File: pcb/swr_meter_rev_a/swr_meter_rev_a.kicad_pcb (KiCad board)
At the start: 2 copper layers, 51.5 x 77 mm, 26 parts, among them P1 BNC, P2 BNC, SW1 Double switch, SW2 2 pos. switch

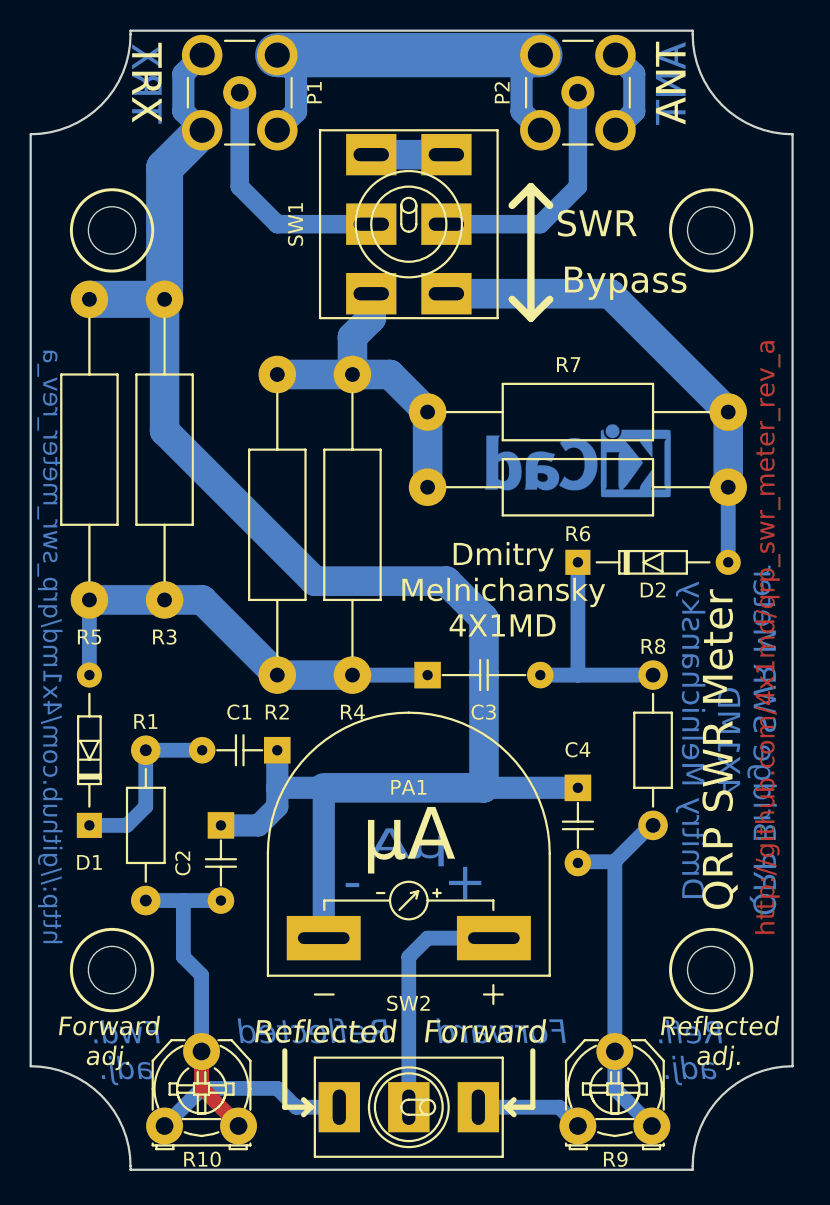
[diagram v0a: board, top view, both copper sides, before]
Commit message: Corrected URLs on the PCB.
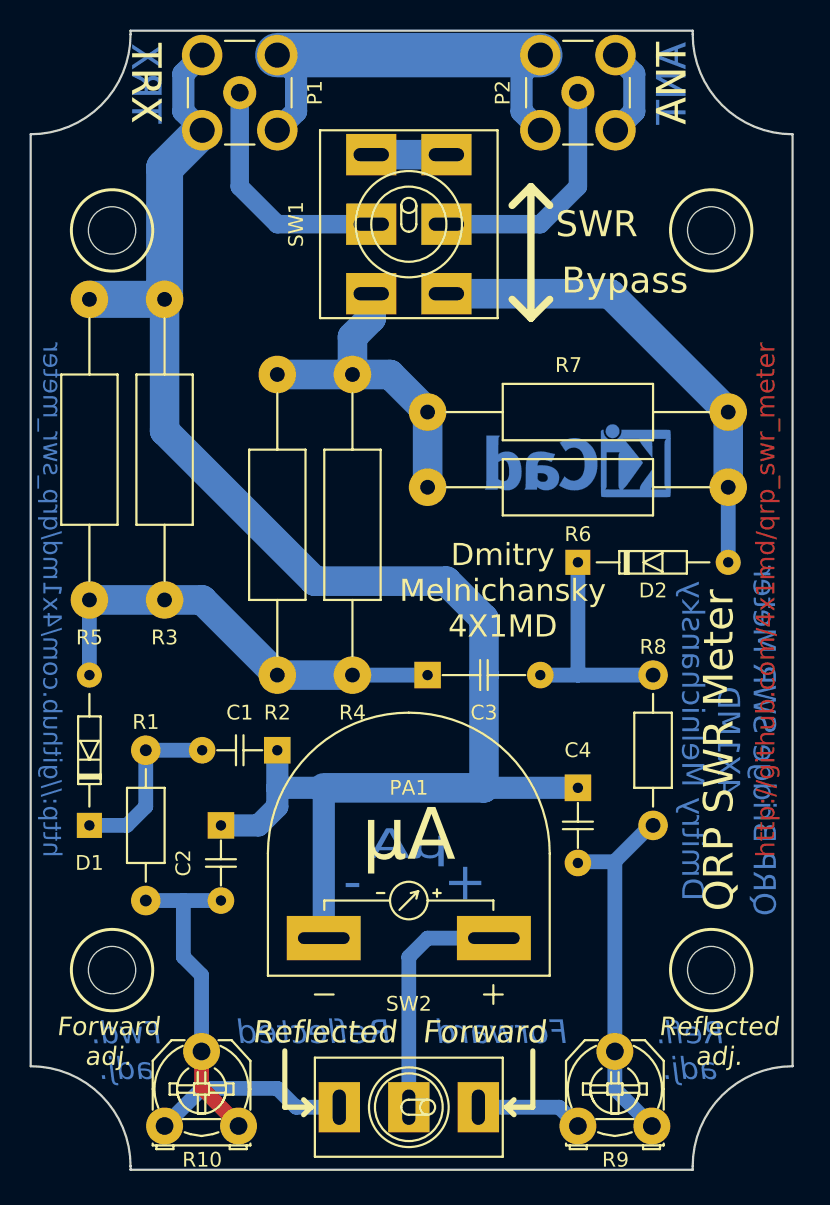
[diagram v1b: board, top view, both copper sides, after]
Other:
- board text added: "http://github.com/4x1md/qrp_swr_meter"
- board text removed: "http://github.com/4x1md/qrp_swr_meter_rev_a"
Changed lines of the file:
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@@
     (links 41)
     (no_connects 2)
-    (area 117.821429 65.374999 169.578571 143.061)
+    (area 117.874999 65.584999 169.525001 142.735001)
     (thickness 1.6)
     (drawings 88)
@@
     (effects (font (size 2 2) (thickness 0.3)))
   )
-  (gr_text http://github.com/4x1md/qrp_swr_meter_rev_a (at 167.64 106.68 90) (layer F.Cu)
+  (gr_text http://github.com/4x1md/qrp_swr_meter (at 167.64 104.14 90) (layer F.Cu)
     (effects (font (size 1.25 1.25) (thickness 0.25)))
   )
@@
     (effects (font (size 2 2) (thickness 0.4)) (justify mirror))
   )
-  (gr_text http://github.com/4x1md/qrp_swr_meter_rev_a (at 119.38 107.315 270) (layer B.Cu)
+  (gr_text http://github.com/4x1md/qrp_swr_meter (at 119.38 104.14 270) (layer B.Cu)
     (effects (font (size 1.25 1.25) (thickness 0.25)) (justify mirror))
   )

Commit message: Silkprint corrections and new gerbers.
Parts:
- moved R8 2.54 mm to (160.0, 111.8)
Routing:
- net Net-(C4-Pad2): track 25.1 -> 24.0 mm
- net Net-(C3-Pad2): track 15.1 -> 16.2 mm
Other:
- board text added: "QRP SWR Meter Rev. A"
- board text removed: "Dmitry Melnichansky 4X1MD"
- board text removed: "QRP SWR Meter"
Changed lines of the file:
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@@
     (area 117.874999 65.584999 169.525001 142.735001)
     (thickness 1.6)
-    (drawings 88)
-    (tracks 89)
+    (drawings 87)
+    (tracks 90)
     (zones 0)
     (modules 26)
@@
   )
   (setup
-    (last_trace_width 0.25)
+    (last_trace_width 1)
     (user_trace_width 0.5)
     (user_trace_width 0.75)
@@
   (module custom_kicad_footprints:Microampermeter (layer F.Cu)
     (at 143.51 127)
-    (fp_text reference PA1 (at 0 -10.16) (layer F.SilkS)
+    (fp_text reference PA1 (at 0 3.81) (layer F.SilkS)
       (effects (font (size 1 1) (thickness 0.15)))
     )
@@
   )
   (module Resistors_ThroughHole:Resistor_Horizontal_RM10mm (layer F.Cu)
-    (at 160.02 109.22 270)
+    (at 160.02 111.76 270)
     (descr "Resistor, Axial,  RM 10mm, 1/3W")
     (tags "Resistor Axial RM 10mm 1/3W")
@@
     (descr "Tumbler Switch x2")
     (tags "SWITCH DEV TOGGLE ILLUM SPDT")
-    (fp_text reference SW2 (at 0 6.985 360) (layer F.SilkS)
+    (fp_text reference SW2 (at 6.985 2 270) (layer F.SilkS)
       (effects (font (size 1 1) (thickness 0.15)))
     )
@@
     (descr "Tumbler Switch x2")
     (tags "SWITCH DEV TOGGLE ILLUM SPDT")
-    (fp_text reference SW1 (at 0 7.62 270) (layer F.SilkS)
+    (fp_text reference SW1 (at -7.62 0 360) (layer F.SilkS)
       (effects (font (size 1 1) (thickness 0.15)))
     )
@@
     (descr "Diode, DO-35,  SOD27, Horizontal, RM 10mm")
     (tags "Diode, DO-35, SOD27, Horizontal, RM 10mm, 1N4148,")
-    (fp_text reference D2 (at 5.08 1.905) (layer F.SilkS)
+    (fp_text reference D2 (at 5.08 -1.905) (layer F.SilkS)
       (effects (font (size 1 1) (thickness 0.15)))
     )
@@
     (descr "Resistor, Axial, RM 20mm,")
     (tags "Resistor Axial RM 20mm")
-    (fp_text reference R2 (at 22.86 0 360) (layer F.SilkS)
+    (fp_text reference R2 (at -2.54 0 360) (layer F.SilkS)
       (effects (font (size 1 1) (thickness 0.15)))
     )
@@
     (descr "Resistor, Axial, RM 20mm,")
     (tags "Resistor Axial RM 20mm")
-    (fp_text reference R4 (at 22.86 0 360) (layer F.SilkS)
+    (fp_text reference R4 (at -2.54 0 360) (layer F.SilkS)
       (effects (font (size 1 1) (thickness 0.15)))
     )
@@
     (descr "Resistor, Axial, RM 20mm,")
     (tags "Resistor Axial RM 20mm")
-    (fp_text reference R7 (at 10.795 3.175 180) (layer F.SilkS)
+    (fp_text reference R7 (at 10.16 3.175 180) (layer F.SilkS)
       (effects (font (size 1 1) (thickness 0.15)))
     )
@@
       (xy -2.537313 2.939947) (xy -2.454562 2.96715) (xy -2.376928 2.977424) (xy -2.273043 2.973429)) (layer B.Cu) (width 0.01))
   )
+  (gr_line (start 152.4 83.185) (end 151.765 85.09) (angle 90) (layer F.SilkS) (width 0.5))
+  (gr_line (start 151.13 83.185) (end 151.765 85.09) (angle 90) (layer F.SilkS) (width 0.5))
+  (gr_line (start 151.765 76.2) (end 152.4 78.105) (angle 90) (layer F.SilkS) (width 0.5))
+  (gr_line (start 151.765 76.2) (end 151.13 78.105) (angle 90) (layer F.SilkS) (width 0.5))
+  (gr_line (start 151.13 138.811) (end 150.368 138.43) (angle 90) (layer F.SilkS) (width 0.35))
+  (gr_line (start 150.368 138.43) (end 151.13 138.049) (angle 90) (layer F.SilkS) (width 0.35))
+  (gr_line (start 135.89 138.811) (end 136.652 138.43) (angle 90) (layer F.SilkS) (width 0.35))
+  (gr_line (start 136.652 138.43) (end 135.89 138.049) (angle 90) (layer F.SilkS) (width 0.35))
   (gr_line (start 129.54 104.14) (end 128.905 104.14) (angle 90) (layer B.Mask) (width 0.5))
   (gr_line (start 133.35 107.95) (end 129.54 104.14) (angle 90) (layer B.Mask) (width 0.5))
@@
   (gr_line (start 137.16 66.675) (end 149.86 66.675) (angle 90) (layer B.Mask) (width 0.25))
   (gr_line (start 136.525 109.22) (end 137.795 109.22) (angle 90) (layer B.Mask) (width 0.5))
-  (gr_line (start 135.128 138.43) (end 135.128 134.62) (angle 90) (layer F.SilkS) (width 0.35))
-  (gr_line (start 136.906 138.43) (end 136.398 138.938) (angle 90) (layer F.SilkS) (width 0.35))
-  (gr_line (start 136.906 138.43) (end 136.398 137.922) (angle 90) (layer F.SilkS) (width 0.35))
-  (gr_line (start 136.906 138.43) (end 135.128 138.43) (angle 90) (layer F.SilkS) (width 0.35))
-  (gr_line (start 150.114 138.43) (end 150.622 137.922) (angle 90) (layer F.SilkS) (width 0.35))
-  (gr_line (start 150.114 138.43) (end 150.622 138.938) (angle 90) (layer F.SilkS) (width 0.35))
-  (gr_line (start 151.892 138.43) (end 151.892 134.62) (angle 90) (layer F.SilkS) (width 0.35))
-  (gr_line (start 150.114 138.43) (end 151.892 138.43) (angle 90) (layer F.SilkS) (width 0.35))
-  (gr_line (start 151.765 85.09) (end 153.035 83.82) (angle 90) (layer F.SilkS) (width 0.5))
-  (gr_line (start 150.495 83.82) (end 151.765 85.09) (angle 90) (layer F.SilkS) (width 0.5))
-  (gr_line (start 151.765 76.2) (end 153.035 77.47) (angle 90) (layer F.SilkS) (width 0.5))
-  (gr_line (start 151.765 76.2) (end 150.495 77.47) (angle 90) (layer F.SilkS) (width 0.5))
+  (gr_line (start 134.874 138.43) (end 134.874 134.62) (angle 90) (layer F.SilkS) (width 0.35))
+  (gr_line (start 136.652 138.43) (end 134.874 138.43) (angle 90) (layer F.SilkS) (width 0.35))
+  (gr_line (start 152.146 138.43) (end 152.146 134.62) (angle 90) (layer F.SilkS) (width 0.35))
+  (gr_line (start 150.368 138.43) (end 152.146 138.43) (angle 90) (layer F.SilkS) (width 0.35))
   (gr_line (start 151.765 85.09) (end 151.765 76.2) (angle 90) (layer F.SilkS) (width 0.5))
   (gr_text "Reflected\nadj." (at 164.465 133.985) (layer F.SilkS)
@@
   )
   (gr_text "QRP Bridge SWR Meter\n4X1MD\nDmitry Melnichansky" (at 165.1 113.665 270) (layer B.Cu)
-    (effects (font (size 1.5 1.5) (thickness 0.3)) (justify mirror))
+    (effects (font (size 1.5 1.5) (thickness 0.25)) (justify mirror))
   )
   (gr_text "Refl.\nadj." (at 162.56 134.62) (layer B.Cu)
@@
     (effects (font (size 2.54 2.54) (thickness 0.3)) (justify mirror))
   )
-  (gr_text "Dmitry\nMelnichansky\n4X1MD" (at 149.86 103.505) (layer F.SilkS)
-    (effects (font (size 1.5 1.5) (thickness 0.3)))
+  (gr_text "QRP SWR Meter\nRev. A" (at 153.67 105.41) (layer F.Cu)
+    (effects (font (size 1.75 1.75) (thickness 0.3)))
   )
   (gr_text Reflected (at 137.16 133.35) (layer B.Cu)
@@
     (effects (font (size 1.6 1.6) (thickness 0.3) italic) (justify mirror))
   )
-  (gr_text "QRP SWR Meter" (at 164.465 114.3 90) (layer F.SilkS)
-    (effects (font (size 2 2) (thickness 0.3)))
-  )
   (gr_text http://github.com/4x1md/qrp_swr_meter (at 167.64 104.14 90) (layer F.Cu)
     (effects (font (size 1.25 1.25) (thickness 0.25)))
@@
     (effects (font (size 2 2) (thickness 0.3)))
   )
-  (gr_text Bypass (at 158.115 82.55) (layer F.SilkS)
+  (gr_text Bypass (at 158.115 83.185) (layer F.SilkS)
     (effects (font (size 1.75 1.75) (thickness 0.3)))
   )
-  (gr_text SWR (at 156.21 78.74) (layer F.SilkS)
+  (gr_text SWR (at 156.21 78.105) (layer F.SilkS)
     (effects (font (size 1.75 1.75) (thickness 0.3)))
   )
@@
     (effects (font (size 1.5 1.5) (thickness 0.3) italic))
   )
-  (gr_text Forward (at 148.59 133.35) (layer F.SilkS)
+  (gr_text Forward (at 149.86 133.35) (layer F.SilkS)
     (effects (font (size 1.5 1.5) (thickness 0.3) italic))
   )
@@
   (segment (start 127 92.71) (end 137.16 102.87) (width 2) (layer B.Cu) (net 1))
   (segment (start 121.92 83.82) (end 127 83.82) (width 2.5) (layer B.Cu) (net 1))
+  (segment (start 121.91746 119.37948) (end 121.91746 115.57254) (width 1) (layer B.Cu) (net 2))
+  (segment (start 123.19 114.3) (end 125.73 114.3) (width 1) (layer B.Cu) (net 2))
+  (segment (start 121.91746 115.57254) (end 123.19 114.3) (width 1) (layer B.Cu) (net 2))
   (segment (start 125.73 114.3) (end 129.54 114.3) (width 1) (layer B.Cu) (net 2))
-  (segment (start 121.91746 119.37948) (end 124.45948 119.37948) (width 1) (layer B.Cu) (net 2))
-  (segment (start 125.73 118.10896) (end 125.73 114.3) (width 1) (layer B.Cu) (net 2))
-  (segment (start 124.45948 119.37948) (end 125.73 118.10896) (width 1) (layer B.Cu) (net 2))
   (segment (start 130.81 124.46) (end 128.27 124.46) (width 1) (layer B.Cu) (net 3))
   (segment (start 129.49936 134.66064) (end 129.49936 129.49936) (width 1) (layer B.Cu) (net 3))
@@
   (segment (start 121.91746 104.14254) (end 121.92 104.14) (width 0.75) (layer B.Cu) (net 4))
   (segment (start 121.92 104.14) (end 127 104.14) (width 2) (layer B.Cu) (net 4))
-  (segment (start 157.43936 134.66064) (end 157.43936 121.87936) (width 1) (layer B.Cu) (net 5))
+  (segment (start 160.02 121.92) (end 157.43936 121.92) (width 1) (layer B.Cu) (net 5))
+  (segment (start 157.43936 134.66064) (end 157.43936 121.92) (width 1) (layer B.Cu) (net 5))
+  (segment (start 157.43936 121.92) (end 157.43936 121.87936) (width 1) (layer B.Cu) (net 5))
   (segment (start 157.43936 121.87936) (end 157.4 121.84) (width 0.75) (layer B.Cu) (net 5))
   (segment (start 154.94 121.84) (end 157.4 121.84) (width 1) (layer B.Cu) (net 5))
-  (segment (start 157.4 121.84) (end 159.86 119.38) (width 1) (layer B.Cu) (net 5))
-  (segment (start 159.86 119.38) (end 160.02 119.38) (width 0.75) (layer B.Cu) (net 5))
   (segment (start 157.48 134.62) (end 157.43936 134.66064) (width 0.75) (layer B.Cu) (net 5))
   (segment (start 157.43936 134.66064) (end 157.43936 137.20064) (width 1) (layer B.Cu) (net 5))
@@
   (segment (start 144.78 96.52) (end 144.78 91.44) (width 2) (layer B.Cu) (net 10))
   (segment (start 134.62 88.9) (end 139.7 88.9) (width 2) (layer B.Cu) (net 10))
+  (segment (start 160.02 111.76) (end 157.48 109.22) (width 1) (layer B.Cu) (net 11))
+  (segment (start 157.48 109.22) (end 154.94052 109.22) (width 1) (layer B.Cu) (net 11))
   (segment (start 154.94052 101.59746) (end 154.94052 109.22) (width 1) (layer B.Cu) (net 11))
   (segment (start 152.53 109.22) (end 154.94052 109.22) (width 1) (layer B.Cu) (net 11))
-  (segment (start 154.94052 109.22) (end 160.02 109.22) (width 1) (layer B.Cu) (net 11))
   (segment (start 157.1 83.44) (end 165.1 91.44) (width 2) (layer B.Cu) (net 12))
   (segment (start 146.05 83.44) (end 157.1 83.44) (width 2) (layer B.Cu) (net 12))
